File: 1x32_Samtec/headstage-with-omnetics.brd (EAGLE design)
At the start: 22.1 x 24.3 mm, 15 parts, among them U1 RHD2132_QFN

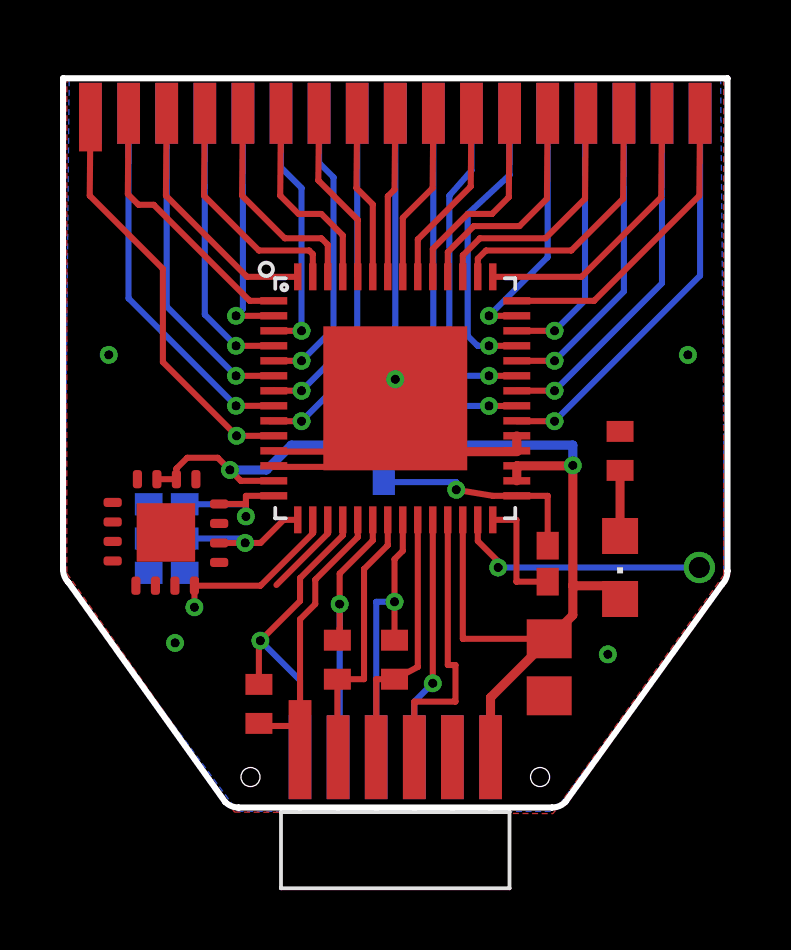
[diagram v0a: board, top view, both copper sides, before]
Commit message: Fixed previous commit where the primary Samtec connector got messed up
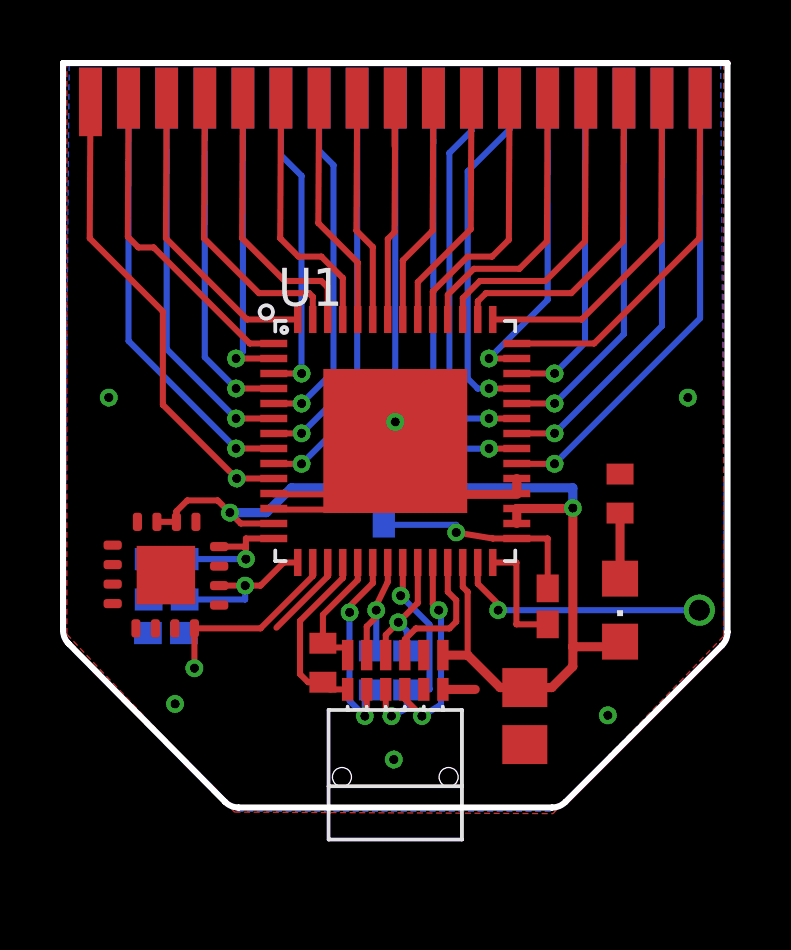
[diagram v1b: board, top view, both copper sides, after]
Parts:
- S2: value RHD2000-CABLE-AMP-SIDEMILLMAX -> RHD2000-CABLE-AMP-SIDE; device RHD2000:MILLMAX-12PIN -> RHD2000:OMNETICS_PZN-12-AA
- moved S2 4.67 mm to (11.0, 2.64)
- moved R1 2.54 mm to (8.59, 4.55), turned to 90 degrees
- moved C_Y 2.03 mm to (3.38, 6.65)
- moved C_Z 2.01 mm to (3.35, 5.54)
- moved C_X 1.83 mm to (3.38, 8.00)
- moved C_VDD 1.82 mm to (15.3, 2.77)
- moved C_REF 1.42 mm to (16.1, 6.43)
- moved U$1 1.42 mm to (3.35, 7.47)
- moved C_A 1.42 mm to (10.6, 9.78)
- moved LED1 1.42 mm to (18.5, 6.30)
- moved RLED 1.42 mm to (18.5, 10.2)
- moved U1 1.42 mm to (11.0, 11.9)
- moved R2 1.22 mm to (10.2, 4.29), flipped to the bottom, turned to 90 degrees
- moved R3 0.54 mm to (11.4, 4.29), flipped to the bottom, turned to 90 degrees
- moved U$2 0.51 mm to (11.0, 23.4)
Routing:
- net CS+: track 9.86 -> 4.36 mm
- net MISO1+: track 9.54 -> 4.57 mm
- net CS-: track 11.1 -> 6.11 mm, vias 1 -> 0
- net SCLK+: track 9.16 -> 4.72 mm, vias 0 -> 1
- net VDD: track 39.1 -> 34.7 mm
- net MOSI+: track 8.99 -> 4.60 mm, vias 0 -> 1
- net IN0: track 12.8 -> 15.7 mm
- net MOSI-: track 9.92 -> 7.59 mm, vias 1 -> 2
- net SCLK-: track 9.63 -> 7.54 mm, vias 1 -> 2
- net IN28: track 11.0 -> 12.9 mm
- net IN25: track 8.32 -> 10.2 mm
- net IN6: track 8.46 -> 10.4 mm
- net IN30: track 12.3 -> 14.2 mm
- net IN3: track 11.0 -> 12.9 mm
- net IN27: track 10.5 -> 12.4 mm
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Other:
- board size 22.1 x 24.3 mm -> 22.1 x 24.8 mm
- board text added: "may 2013"
- board text added: "rev 2.0 samtec"
- board text removed: "Sept 2013"
- board text removed: "rev 2.1 samtec"
